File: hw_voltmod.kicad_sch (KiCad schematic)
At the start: 7 parts, among them J101 Conn_01x09_Pin, U104 L78L33_SO8

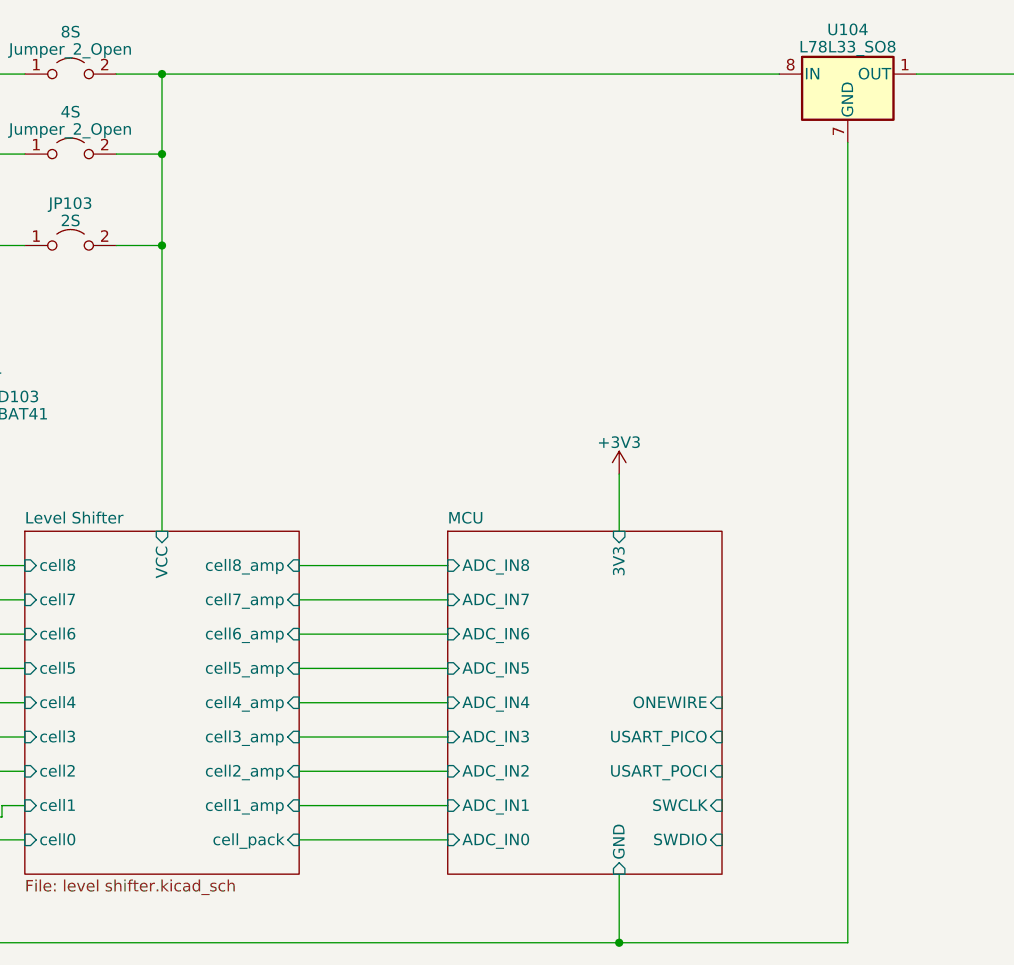
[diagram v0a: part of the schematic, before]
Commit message: capacitor added to ldr
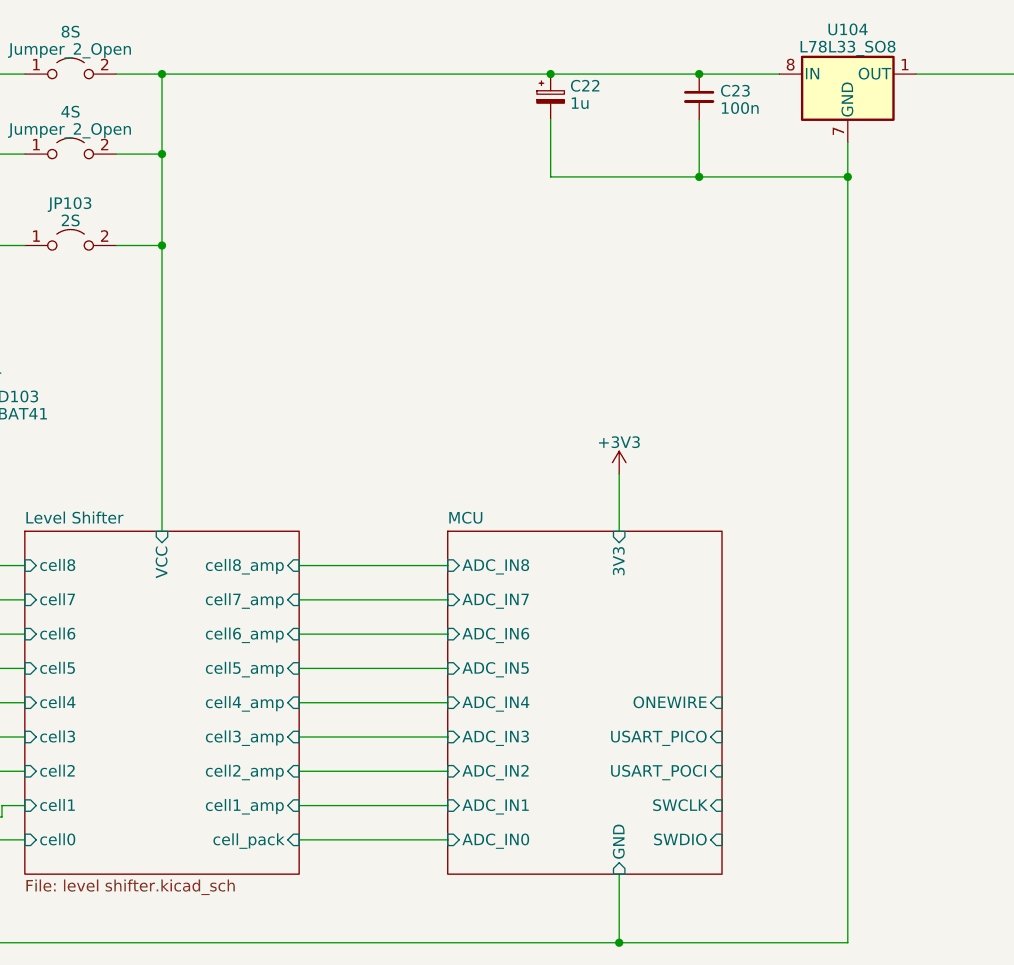
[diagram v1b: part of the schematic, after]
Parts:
- added C22: 1u, Capacitor_SMD:CP_Elec_5x3, symbol Device:C_Polarized_Small
- added C23: 100n, Capacitor_SMD:C_0603_1608Metric_Pad1.08x0.95mm_HandSolder, symbol Device:C_Small
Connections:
- net Level Shifter/VCC: now also C22.1, C23.1
- net Level Shifter/cell0: now also C22.2, C23.2
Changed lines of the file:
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@@
 (kicad_sch (version 20230121) (generator eeschema)
   (paper "A4")
+  (junction (at 182.88 43.18) (diameter 0) (color 0 0 0 0)
+  )
+  (junction (at 199.39 54.61) (diameter 0) (color 0 0 0 0)
+  )
   (junction (at 87.63 97.79) (diameter 0) (color 0 0 0 0)
   )
@@
   (junction (at 173.99 139.7) (diameter 0) (color 0 0 0 0)
   )
+  (junction (at 166.37 43.18) (diameter 0) (color 0 0 0 0)
+  )
   (junction (at 97.79 113.03) (diameter 0) (color 0 0 0 0)
   )
   (junction (at 123.19 52.07) (diameter 0) (color 0 0 0 0)
   )
+  (junction (at 182.88 54.61) (diameter 0) (color 0 0 0 0)
+  )
   (junction (at 123.19 43.18) (diameter 0) (color 0 0 0 0)
   )
@@
     (stroke (width 0) (type default))
   )
+  (wire (pts (xy 182.88 43.18) (xy 191.77 43.18))
+    (stroke (width 0) (type default))
+  )
   (wire (pts (xy 105.41 125.73) (xy 105.41 124.46))
     (stroke (width 0) (type default))
@@
     (stroke (width 0) (type default))
   )
+  (wire (pts (xy 166.37 43.18) (xy 182.88 43.18))
+    (stroke (width 0) (type default))
+  )
   (wire (pts (xy 123.19 52.07) (xy 123.19 62.23))
     (stroke (width 0) (type default))
   )
-  (wire (pts (xy 123.19 43.18) (xy 191.77 43.18))
+  (wire (pts (xy 123.19 43.18) (xy 166.37 43.18))
     (stroke (width 0) (type default))
   )
@@
     (stroke (width 0) (type default))
   )
+  (wire (pts (xy 166.37 54.61) (xy 182.88 54.61))
+    (stroke (width 0) (type default))
+  )
   (wire (pts (xy 118.11 62.23) (xy 123.19 62.23))
     (stroke (width 0) (type default))
@@
     (stroke (width 0) (type default))
   )
+  (wire (pts (xy 182.88 54.61) (xy 199.39 54.61))
+    (stroke (width 0) (type default))
+  )
   (wire (pts (xy 97.79 78.74) (xy 97.79 113.03))
     (stroke (width 0) (type default))
@@
     (stroke (width 0) (type default))
   )
-  (wire (pts (xy 199.39 50.8) (xy 199.39 139.7))
+  (wire (pts (xy 199.39 50.8) (xy 199.39 54.61))
     (stroke (width 0) (type default))
   )
@@
     (stroke (width 0) (type default))
   )
+  (wire (pts (xy 199.39 54.61) (xy 199.39 139.7))
+    (stroke (width 0) (type default))
+  )
   (wire (pts (xy 100.33 116.84) (xy 107.95 116.84))
     (stroke (width 0) (type default))
@@
     (stroke (width 0) (type default))
   )
+  (wire (pts (xy 166.37 48.26) (xy 166.37 54.61))
+    (stroke (width 0) (type default))
+  )
   (wire (pts (xy 105.41 124.46) (xy 107.95 124.46))
     (stroke (width 0) (type default))
@@
   )
   (wire (pts (xy 138.43 120.65) (xy 154.94 120.65))
+    (stroke (width 0) (type default))
+  )
+  (wire (pts (xy 182.88 48.26) (xy 182.88 54.61))
     (stroke (width 0) (type default))
   )
@@
     )
   )
+  (symbol (lib_id "Device:C_Small") (at 182.88 45.72 0) (unit 1)
+    (in_bom yes) (on_board yes) (dnp no) (fields_autoplaced)
+    (property "Reference" "C23" (at 185.2041 45.0826 0)
+      (effects (font (size 1.27 1.27)) (justify left))
+    )
+    (property "Value" "100n" (at 185.2041 47.0036 0)
+      (effects (font (size 1.27 1.27)) (justify left))
+    )
+    (property "Footprint" "Capacitor_SMD:C_0603_1608Metric_Pad1.08x0.95mm_HandSolder" (at 182.88 45.72 0)
+      (effects (font (size 1.27 1.27)) hide)
+    )
+    (property "Datasheet" "~" (at 182.88 45.72 0)
+      (effects (font (size 1.27 1.27)) hide)
+    )
+    (pin "1")
+    (pin "2")
+    (instances
+      (project "hw_voltmod"
+        (path "/aba5ff33-6d0a-4fec-b36e-20121d176c3c"
+          (reference "C23") (unit 1)
+        )
+      )
+    )
+  )
   (symbol (lib_id "Diode:BAT41") (at 102.87 80.01 270) (unit 1)
     (in_bom yes) (on_board yes) (dnp no) (fields_autoplaced)
@@
         )
       )
+    )
+  )
+  (symbol (lib_id "Device:C_Polarized_Small") (at 166.37 45.72 0) (unit 1)
+    (in_bom yes) (on_board yes) (dnp no) (fields_autoplaced)
+    (property "Reference" "C22" (at 168.529 44.5302 0)
+      (effects (font (size 1.27 1.27)) (justify left))
+    )
+    (property "Value" "1u" (at 168.529 46.4512 0)
+      (effects (font (size 1.27 1.27)) (justify left))
+    )
+    (property "Footprint" "Capacitor_SMD:CP_Elec_5x3" (at 166.37 45.72 0)
+      (effects (font (size 1.27 1.27)) hide)
+    )
+    (property "Datasheet" "~" (at 166.37 45.72 0)
+      (effects (font (size 1.27 1.27)) hide)
+    )
+    (pin "1")
+    (pin "2")
+    (instances
+      (project "hw_voltmod"
+        (path "/aba5ff33-6d0a-4fec-b36e-20121d176c3c"
+          (reference "C22") (unit 1)
+        )
+      )

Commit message: Update hw_voltmod.kicad_sch
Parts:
- added C24: 100n, Capacitor_SMD:C_0603_1608Metric_Pad1.08x0.95mm_HandSolder, symbol Device:C_Small
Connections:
- net +3V3: now also C24.1
- net Level Shifter/cell0: now also C24.2
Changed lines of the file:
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@@
   (junction (at 123.19 62.23) (diameter 0) (color 0 0 0 0)
   )
+  (junction (at 212.09 43.18) (diameter 0) (color 0 0 0 0)
+  )
   (junction (at 102.87 128.27) (diameter 0) (color 0 0 0 0)
   )
@@
     (stroke (width 0) (type default))
   )
-  (wire (pts (xy 207.01 43.18) (xy 220.98 43.18))
+  (wire (pts (xy 207.01 43.18) (xy 212.09 43.18))
     (stroke (width 0) (type default))
   )
@@
     (stroke (width 0) (type default))
   )
+  (wire (pts (xy 212.09 48.26) (xy 212.09 54.61))
+    (stroke (width 0) (type default))
+  )
   (wire (pts (xy 199.39 139.7) (xy 173.99 139.7))
     (stroke (width 0) (type default))
@@
     (stroke (width 0) (type default))
   )
+  (wire (pts (xy 199.39 54.61) (xy 212.09 54.61))
+    (stroke (width 0) (type default))
+  )
   (wire (pts (xy 90.17 101.6) (xy 107.95 101.6))
     (stroke (width 0) (type default))
@@
   )
   (wire (pts (xy 138.43 101.6) (xy 154.94 101.6))
+    (stroke (width 0) (type default))
+  )
+  (wire (pts (xy 212.09 43.18) (xy 220.98 43.18))
     (stroke (width 0) (type default))
   )
@@
         )
       )
+    )
+  )
+  (symbol (lib_id "Device:C_Small") (at 212.09 45.72 0) (unit 1)
+    (in_bom yes) (on_board yes) (dnp no) (fields_autoplaced)
+    (property "Reference" "C24" (at 214.4141 45.0826 0)
+      (effects (font (size 1.27 1.27)) (justify left))
+    )
+    (property "Value" "100n" (at 214.4141 47.0036 0)
+      (effects (font (size 1.27 1.27)) (justify left))
+    )
+    (property "Footprint" "Capacitor_SMD:C_0603_1608Metric_Pad1.08x0.95mm_HandSolder" (at 212.09 45.72 0)
+      (effects (font (size 1.27 1.27)) hide)
+    )
+    (property "Datasheet" "~" (at 212.09 45.72 0)
+      (effects (font (size 1.27 1.27)) hide)
+    )
+    (pin "1")
+    (pin "2")
+    (instances
+      (project "hw_voltmod"
+        (path "/aba5ff33-6d0a-4fec-b36e-20121d176c3c"
+          (reference "C24") (unit 1)
+        )
+      )

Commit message: asdf
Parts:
- removed 4S, 8S: Jumper_2_Open, symbol Jumper:Jumper_2_Open
- added C29: 100n, Capacitor_SMD:C_0603_1608Metric_Pad1.08x0.95mm_HandSolder, symbol Device:C_Small
- added DS18: Conn_01x02_Pin, symbol Connector:Conn_01x02_Pin
- added FTDI: Conn_01x06_Pin, symbol Connector:Conn_01x06_Pin
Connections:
- net +3V3: now also C29.2, FTDI.4 (Pin_4)
- net Level Shifter/cell8: now also D101.1 (K), D103.1 (K), JP103.1 (A)
- net MCU/ONEWIRE: now also DS18.1 (Pin_1)
- net MCU/USART_PICO: now also FTDI.2 (Pin_2)
- net MCU/USART_POCI: now also FTDI.3 (Pin_3)
- net Level Shifter/VCC renamed VBUS
- net Level Shifter/cell0 renamed GNDD
- net GNDD: now also C29.1, DS18.2 (Pin_2), FTDI.6 (Pin_6)
- new net RS485iso/DEN: FTDI.5 (Pin_5)
- new net RS485iso/REN: FTDI.1 (Pin_1)
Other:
- added sheet RS485iso (RS485iso.kicad_sch)
- note added: "GND CTS VCC TX RX DTR"
- moved on the sheet: C22, C23, C24, D101, D103, U104

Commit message: asdf
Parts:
- added J3: Conn_01x04_Pin, symbol Connector:Conn_01x04_Pin
- added J4: Conn_01x05_Pin, symbol Connector:Conn_01x05_Pin
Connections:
- net +3V3: now also J4.2 (Pin_2)
- net GNDD: now also J4.5 (Pin_5)
- net MCU/ONEWIRE renamed ONEWIRE
- net MCU/USART_PICO renamed USART_PICO
- net MCU/USART_POCI renamed USART_POCI
- net RS485iso/DEN renamed REN
- net RS485iso/REN renamed DEN
- new net +5V: J4.1 (Pin_1)
- new net SWCLK: J4.4 (Pin_4)
- new net SWDIO: J4.3 (Pin_3)
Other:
- sheet MCU ports: added DEN, REN; removed none
- moved on the sheet: C29, DS18, FTDI

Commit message: tzutz
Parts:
- removed C29: 100n, Capacitor_SMD:C_0603_1608Metric_Pad1.08x0.95mm_HandSolder, symbol Device:C_Small
- removed FTDI: Conn_01x06_Pin, symbol Connector:Conn_01x06_Pin
- added D101 (x3): BAT41, Diode_THT:D_DO-35_SOD27_P7.62mm_Horizontal, symbol Diode:BAT41
- added R704 (x2): 0, Resistor_SMD:R_0603_1608Metric_Pad0.98x0.95mm_HandSolder, symbol Device:R
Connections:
- net +3V3: now also J3.1 (Pin_1)
- net +5V: now also D101.2 (A)
- net GNDD: now also J3.4 (Pin_4)
- net Level Shifter/cell6: now also D101.2 (A)
- net Level Shifter/cell8: now also D101.2 (A); no longer D101.1 (K), D103.1 (K), JP103.1 (A)
- net USART_PICO: now also J3.3 (Pin_3), R704.2
- net USART_POCI: now also J3.2 (Pin_2), R704.1
- new net: D101.1 (K), D101.1 (K), D101.1 (K), D101.1 (K), D103.1 (K), JP103.1 (A)
- new net MCU/USART_PICO: R704.1
- new net MCU/USART_POCI: R704.2
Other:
- removed sheet RS485iso
- note added: "BMS"
- note added: "ONE WIRE"
- note added: "RS485 MODULE XY-017"
- note added: "SWD"
- note removed: "GND CTS VCC TX RX DTR"
- moved on the sheet: D103, DS18, J3, J4

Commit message: aisler DRC und preise
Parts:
- removed C22: 1u, Capacitor_SMD:CP_Elec_5x3, symbol Device:C_Polarized_Small
- removed D101 (x4), D103: BAT41, Diode_THT:D_DO-35_SOD27_P7.62mm_Horizontal, symbol Diode:BAT41
- added C1: 1u, Capacitor_SMD:C_1206_3216Metric_Pad1.33x1.80mm_HandSolder, symbol Device:C_Small
- added D? (x9): BAT41, Diode_SMD:D_0805_2012Metric_Pad1.15x1.40mm_HandSolder, symbol Diode:BAT41
- DS1: renamed from DS18; footprint (none) -> Connector_JST:JST_XH_B2B-XH-A_1x02_P2.50mm_Vertical
- J2: renamed from J4; footprint (none) -> Connector_JST:JST_XH_B5B-XH-A_1x05_P2.50mm_Vertical
- J3: footprint (none) -> Connector_JST:JST_XH_B4B-XH-AM_1x04_P2.50mm_Vertical
- J?: renamed from J101; footprint (none) -> Connector_JST:JST_XH_S9B-XH-A_1x09_P2.50mm_Horizontal
- JP?: renamed from JP103; footprint (none) -> Connector_PinSocket_2.54mm:PinSocket_1x02_P2.54mm_Vertical
- renumbered C23 to C2, C24 to C3, R704 to R?, U104 to U?
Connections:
- net +5V: now also D?.2 (A)
- net GNDD: now also C1.2
- net Level Shifter/cell1: now also D?.2 (A)
- net Level Shifter/cell2: now also D?.2 (A)
- net Level Shifter/cell3: now also D?.2 (A)
- net Level Shifter/cell4: now also D?.2 (A)
- net Level Shifter/cell5: now also D?.2 (A)
- net Level Shifter/cell6: now also D?.2 (A)
- net Level Shifter/cell7: now also D?.2 (A)
- net Level Shifter/cell8: now also D?.2 (A)
- net VBUS: now also C1.1
- net at JP?.1 (A): now also D?.1 (K), D?.1 (K), D?.1 (K), D?.1 (K), D?.1 (K), D?.1 (K), D?.1 (K), D?.1 (K), D?.1 (K)
